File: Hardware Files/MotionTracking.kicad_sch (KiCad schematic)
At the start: 28 parts, among them J1 Micro_SD_Card_Det1, J2 USB_B_Micro, U1 LSM6DSV16XTR, U2 ADP2302ARDZ-3.3, U4 STM32F411RET6, Y1 16MHz

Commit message: Updated Diode Footprints
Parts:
- D1, D2, D3, D4: footprint (none) -> Diode_SMD:D_SOD-323
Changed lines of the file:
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@@
       (effects (font (size 1.27 1.27)) (justify left))
     )
-    (property "Footprint" "" (at 97.79 40.64 0)
+    (property "Footprint" "Diode_SMD:D_SOD-323" (at 97.79 40.64 0)
       (effects (font (size 1.27 1.27)) hide)
     )
@@
       (effects (font (size 1.27 1.27)))
     )
-    (property "Footprint" "" (at 38.1 38.1 0)
+    (property "Footprint" "Diode_SMD:D_SOD-323" (at 38.1 38.1 0)
       (effects (font (size 1.27 1.27)) hide)
     )
@@
       (effects (font (size 1.27 1.27)))
     )
-    (property "Footprint" "" (at 38.1 27.94 0)
+    (property "Footprint" "Diode_SMD:D_SOD-323" (at 38.1 27.94 0)
       (effects (font (size 1.27 1.27)) hide)
     )
@@
       (effects (font (size 1.27 1.27)))
     )
-    (property "Footprint" "" (at 66.04 27.94 0)
-      (effects (font (size 1.27 1.27)) hide)
-    )
+    (property "Footprint" "Diode_SMD:D_SOD-323" (at 66.04 27.94 0)
+      (effects (font (size 1.27 1.27)) hide)
+    )

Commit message: Updated Component Footprints
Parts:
- C1, C10, C11, C12, C2, C3, C4, C5, C6, C7, C8, C9: footprint (none) -> Capacitor_SMD:C_0603_1608Metric_Pad1.08x0.95mm_HandSolder
- L1, L2: footprint (none) -> Inductor_SMD:L_0603_1608Metric_Pad1.05x0.95mm_HandSolder
- R1, R3, Rbot1, Rtop1: footprint (none) -> Resistor_SMD:R_0603_1608Metric_Pad0.98x0.95mm_HandSolder
- Y1: footprint (none) -> Crystal:Crystal_SMD_SeikoEpson_TSX3225-4Pin_3.2x2.5mm_HandSoldering
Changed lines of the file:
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@@
       (effects (font (size 1.27 1.27)))
     )
-    (property "Footprint" "" (at 99.06 53.848 90)
+    (property "Footprint" "Resistor_SMD:R_0603_1608Metric_Pad0.98x0.95mm_HandSolder" (at 99.06 53.848 90)
       (effects (font (size 1.27 1.27)) hide)
     )
@@
       (effects (font (size 1.27 1.27)))
     )
-    (property "Footprint" "" (at 104.14 36.83 0)
+    (property "Footprint" "Inductor_SMD:L_0603_1608Metric_Pad1.05x0.95mm_HandSolder" (at 104.14 36.83 0)
       (effects (font (size 1.27 1.27)) hide)
     )
@@
       (effects (font (size 1.27 1.27)) (justify left))
     )
-    (property "Footprint" "" (at 195.58 38.1 0)
+    (property "Footprint" "Capacitor_SMD:C_0603_1608Metric_Pad1.08x0.95mm_HandSolder" (at 195.58 38.1 0)
       (effects (font (size 1.27 1.27)) hide)
     )
@@
       (effects (font (size 1.27 1.27)) (justify left))
     )
-    (property "Footprint" "" (at 109.22 152.4 0)
+    (property "Footprint" "Capacitor_SMD:C_0603_1608Metric_Pad1.08x0.95mm_HandSolder" (at 109.22 152.4 0)
       (effects (font (size 1.27 1.27)) hide)
     )
@@
       (effects (font (size 1.27 1.27)) (justify left))
     )
-    (property "Footprint" "" (at 57.15 40.132 90)
+    (property "Footprint" "Resistor_SMD:R_0603_1608Metric_Pad0.98x0.95mm_HandSolder" (at 57.15 40.132 90)
       (effects (font (size 1.27 1.27)) hide)
     )
@@
       (effects (font (size 1.27 1.27)) (justify left))
     )
-    (property "Footprint" "" (at 259.08 33.02 0)
+    (property "Footprint" "Capacitor_SMD:C_0603_1608Metric_Pad1.08x0.95mm_HandSolder" (at 259.08 33.02 0)
       (effects (font (size 1.27 1.27)) hide)
     )
@@
       (effects (font (size 1.27 1.27)) (justify left))
     )
-    (property "Footprint" "" (at 78.74 104.14 0)
+    (property "Footprint" "Capacitor_SMD:C_0603_1608Metric_Pad1.08x0.95mm_HandSolder" (at 78.74 104.14 0)
       (effects (font (size 1.27 1.27)) hide)
     )
@@
       (effects (font (size 1.27 1.27)))
     )
-    (property "Footprint" "" (at 241.3 27.94 0)
+    (property "Footprint" "Inductor_SMD:L_0603_1608Metric_Pad1.05x0.95mm_HandSolder" (at 241.3 27.94 0)
       (effects (font (size 1.27 1.27)) hide)
     )
@@
       (effects (font (size 1.27 1.27)) (justify left))
     )
-    (property "Footprint" "" (at 246.38 33.02 0)
+    (property "Footprint" "Capacitor_SMD:C_0603_1608Metric_Pad1.08x0.95mm_HandSolder" (at 246.38 33.02 0)
       (effects (font (size 1.27 1.27)) hide)
     )
@@
       (effects (font (size 1.27 1.27)) (justify left))
     )
-    (property "Footprint" "" (at 89.662 58.42 90)
+    (property "Footprint" "Resistor_SMD:R_0603_1608Metric_Pad0.98x0.95mm_HandSolder" (at 89.662 58.42 90)
       (effects (font (size 1.27 1.27)) hide)
     )
@@
       (effects (font (size 1.27 1.27)) (justify left))
     )
-    (property "Footprint" "" (at 147.32 38.1 0)
+    (property "Footprint" "Capacitor_SMD:C_0603_1608Metric_Pad1.08x0.95mm_HandSolder" (at 147.32 38.1 0)
       (effects (font (size 1.27 1.27)) hide)
     )
@@
       (effects (font (size 1.27 1.27)))
     )
-    (property "Footprint" "" (at 68.58 101.6 0)
+    (property "Footprint" "Crystal:Crystal_SMD_SeikoEpson_TSX3225-4Pin_3.2x2.5mm_HandSoldering" (at 68.58 101.6 0)
       (effects (font (size 1.27 1.27)) hide)
     )
@@
       (effects (font (size 1.27 1.27)) (justify left))
     )
-    (property "Footprint" "" (at 170.18 38.1 0)
+    (property "Footprint" "Capacitor_SMD:C_0603_1608Metric_Pad1.08x0.95mm_HandSolder" (at 170.18 38.1 0)
       (effects (font (size 1.27 1.27)) hide)
     )
@@
       (effects (font (size 1.27 1.27)) (justify left))
     )
-    (property "Footprint" "" (at 157.48 38.1 0)
+    (property "Footprint" "Capacitor_SMD:C_0603_1608Metric_Pad1.08x0.95mm_HandSolder" (at 157.48 38.1 0)
       (effects (font (size 1.27 1.27)) hide)
     )
@@
       (effects (font (size 1.27 1.27)) (justify left))
     )
-    (property "Footprint" "" (at 96.2152 35.56 0)
+    (property "Footprint" "Capacitor_SMD:C_0603_1608Metric_Pad1.08x0.95mm_HandSolder" (at 96.2152 35.56 0)
       (effects (font (size 1.27 1.27)) hide)
     )
@@
       (effects (font (size 1.27 1.27)) (justify left))
     )
-    (property "Footprint" "" (at 182.88 38.1 0)
+    (property "Footprint" "Capacitor_SMD:C_0603_1608Metric_Pad1.08x0.95mm_HandSolder" (at 182.88 38.1 0)
       (effects (font (size 1.27 1.27)) hide)
     )
@@
       (effects (font (size 1.27 1.27)) (justify left))
     )
-    (property "Footprint" "" (at 58.42 104.14 0)
+    (property "Footprint" "Capacitor_SMD:C_0603_1608Metric_Pad1.08x0.95mm_HandSolder" (at 58.42 104.14 0)
       (effects (font (size 1.27 1.27)) hide)
     )
@@
       (effects (font (size 1.27 1.27)) (justify left))
     )
-    (property "Footprint" "" (at 208.28 38.1 0)
+    (property "Footprint" "Capacitor_SMD:C_0603_1608Metric_Pad1.08x0.95mm_HandSolder" (at 208.28 38.1 0)
       (effects (font (size 1.27 1.27)) hide)
     )
@@
       (effects (font (size 1.27 1.27)) (justify left))
     )
-    (property "Footprint" "" (at 78.74 96.52 0)
-      (effects (font (size 1.27 1.27)) hide)
-    )
+    (property "Footprint" "Resistor_SMD:R_0603_1608Metric_Pad0.98x0.95mm_HandSolder" (at 78.74 96.52 0)
+      (effects (font (size 1.27 1.27)) hide)
+    )

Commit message: Actually changed pins this time
did not save before pushing
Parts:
- removed J2: USB_B_Micro, symbol Connector:USB_B_Micro
- added J2: Conn_ST_STDC14, symbol Connector:Conn_ST_STDC14
- C1, C10, C11, C12, C2, C3, C4, C5, C6, C7, C8, C9: footprint Capacitor_SMD:C_0603_1608Metric_Pad1.08x0.95mm_HandSolder -> (none)
- D1, D2, D3, D4: footprint Diode_SMD:D_SOD-323 -> (none)
- L1, L2: footprint Inductor_SMD:L_0603_1608Metric_Pad1.05x0.95mm_HandSolder -> (none)
- R1, R3, Rbot1, Rtop1: footprint Resistor_SMD:R_0603_1608Metric_Pad0.98x0.95mm_HandSolder -> (none)
- Y1: footprint Crystal:Crystal_SMD_SeikoEpson_TSX3225-4Pin_3.2x2.5mm_HandSoldering -> (none)
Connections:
- net GND: now also J2.11 (GNDDetect), J2.5 (GND), J2.7 (GND)
- net NRST: now also J2.12 (~{RST})
- net SWCLK: now also J2.6 (JCLK/SWCLK)
- net SWDIO: now also J2.4 (JTMS/SWDIO)
- net SWO: now also J2.8 (JTDO/SWO)
- net I2C3_SCL: now reaches U4.41 (PA8)
- net I2C1_SCL: now reaches U4.58 (PB6)
- net I2C1_SDA: now reaches U4.59 (PB7)
- net SPI2_MISO: no longer names the net of U4.10 (PC2)
- net SPI2_MOSI: no longer names the net of U4.11 (PC3)
- net SPI3_MISO renamed I2C3_SDA
- net SPI3_MOSI: no longer names the net of U4.53 (PC12)
- new net Vin: J2.3 (VCC)
- no-connect marks 8 -> 7
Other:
- moved on the sheet: C10, C11, R3, Y1

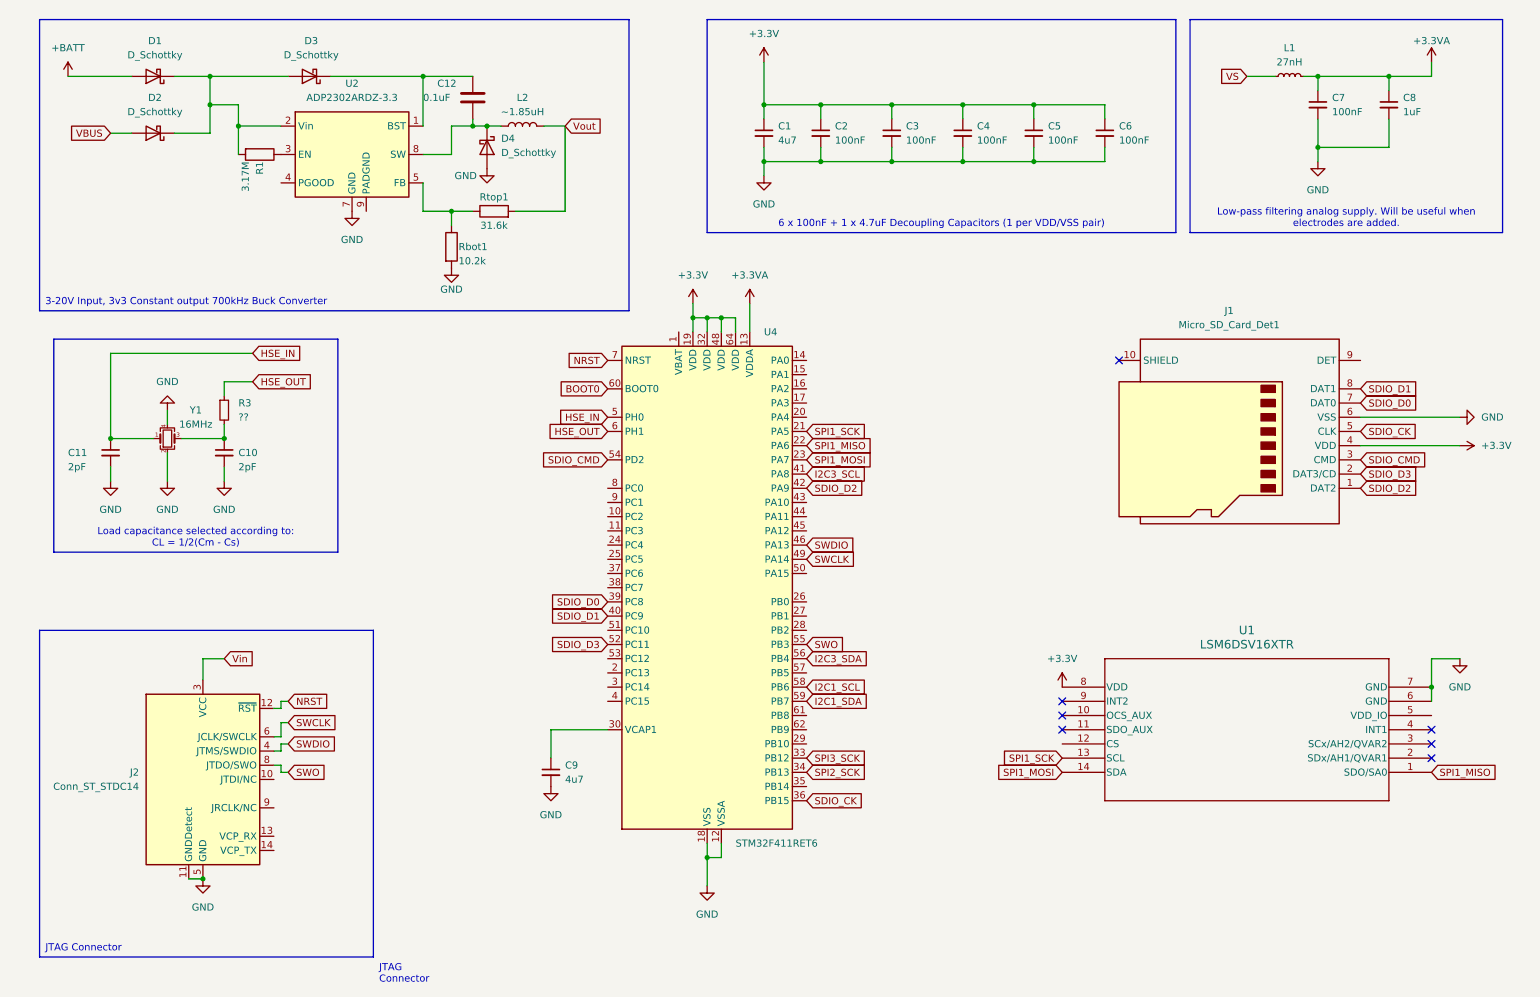
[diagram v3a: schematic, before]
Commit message: Updated I2C with 10k pull ups
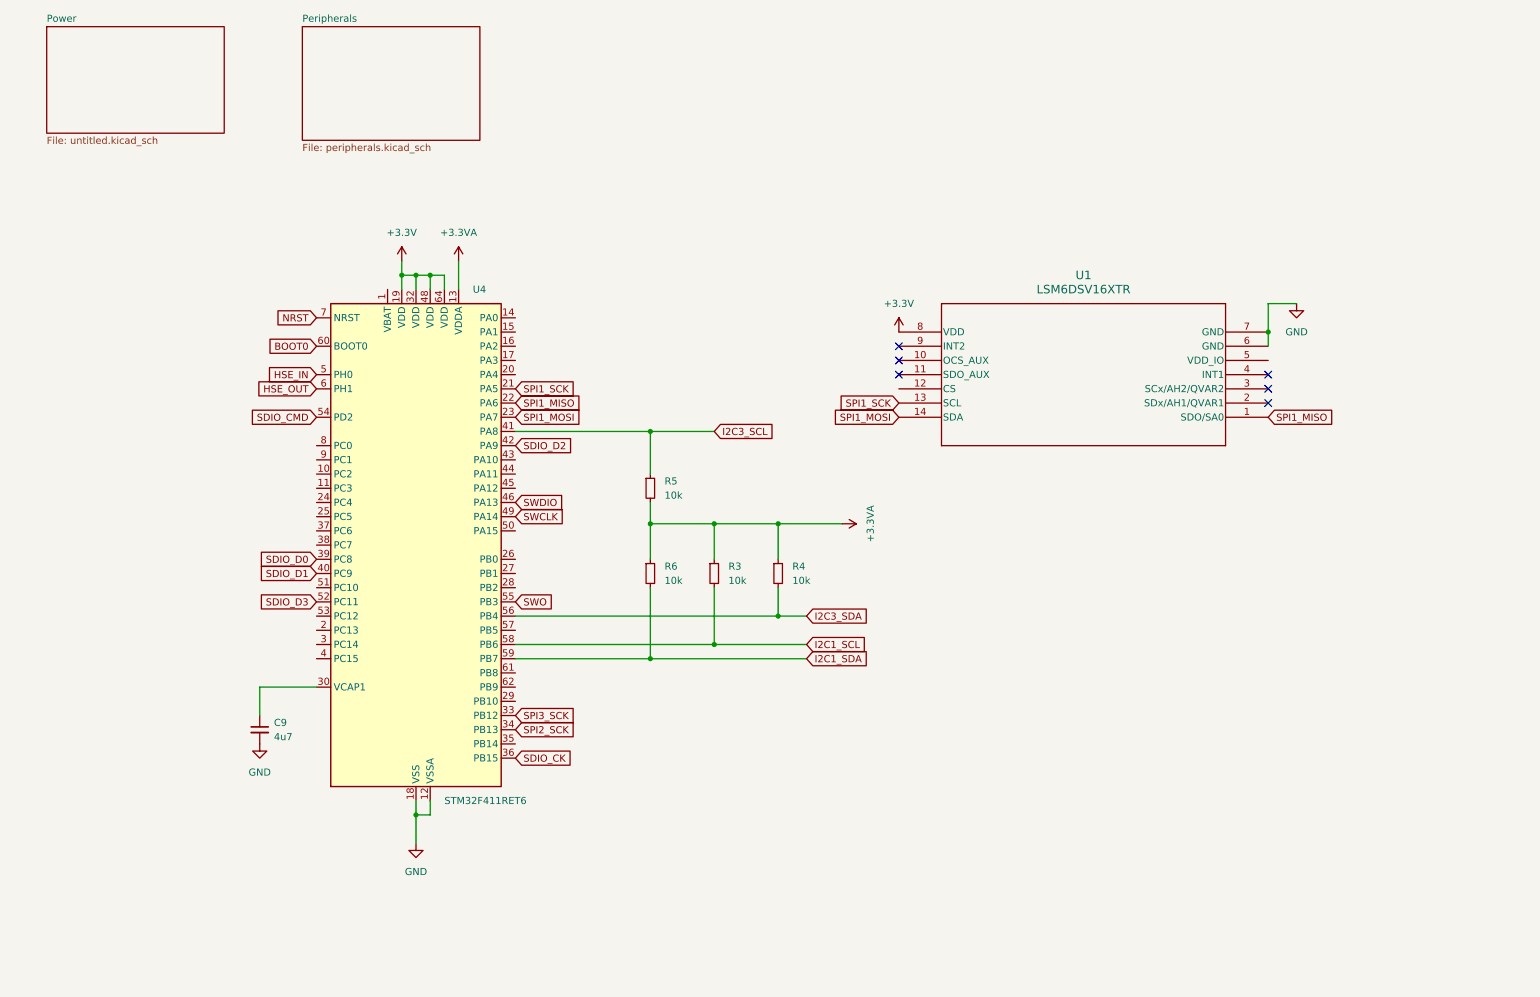
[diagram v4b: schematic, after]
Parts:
- removed C1: 4u7, symbol Device:C_Small
- removed C10, C11: 2pF, symbol Device:C_Small
- removed C12: 0.1uF, symbol Device:C
- removed C2, C3, C4, C5, C6, C7: 100nF, symbol Device:C_Small
- removed C8: 1uF, symbol Device:C_Small
- removed D1, D2, D3, D4: D_Schottky, symbol Device:D_Schottky
- removed J1: Micro_SD_Card_Det1, symbol Connector:Micro_SD_Card_Det1
- removed J2: Conn_ST_STDC14, symbol Connector:Conn_ST_STDC14
- removed L1: 27nH, symbol Device:L_Small
- removed L2: ~1.85uH, symbol Device:L
- removed R1: 3.17M, symbol Device:R
- removed Rbot1: 10.2k, symbol Device:R
- removed Rtop1: 31.6k, symbol Device:R
- removed U2: ADP2302ARDZ-3.3, Package_SO:SOIC-8-1EP_3.9x4.9mm_P1.27mm_EP2.29x3mm, symbol Regulator_Switching:ADP2302ARDZ-3.3
- removed Y1: 16MHz, symbol Device:Crystal_GND24_Small
- added R4, R5, R6: 10k, symbol Device:R_Small
- R3: value ?? -> 10k
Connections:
- net +3.3VA: now also R3.1, R4.1, R5.2, R6.1
- net HSE_OUT: no longer R3.1
- net I2C1_SCL: now also R3.2
- net I2C1_SDA: now also R6.2
- net I2C3_SCL: now also R5.1
- net I2C3_SDA: now also R4.2
- no-connect marks 7 -> 6
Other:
- added sheet Peripherals (peripherals.kicad_sch)
- added sheet Power (untitled.kicad_sch)
- moved on the sheet: C9, U1, U4
